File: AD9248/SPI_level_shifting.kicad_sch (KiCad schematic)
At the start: 9 parts, among them U10 TXB0101DBVR, U11 TXB0101DBVR, U12 TXB0101DBVR

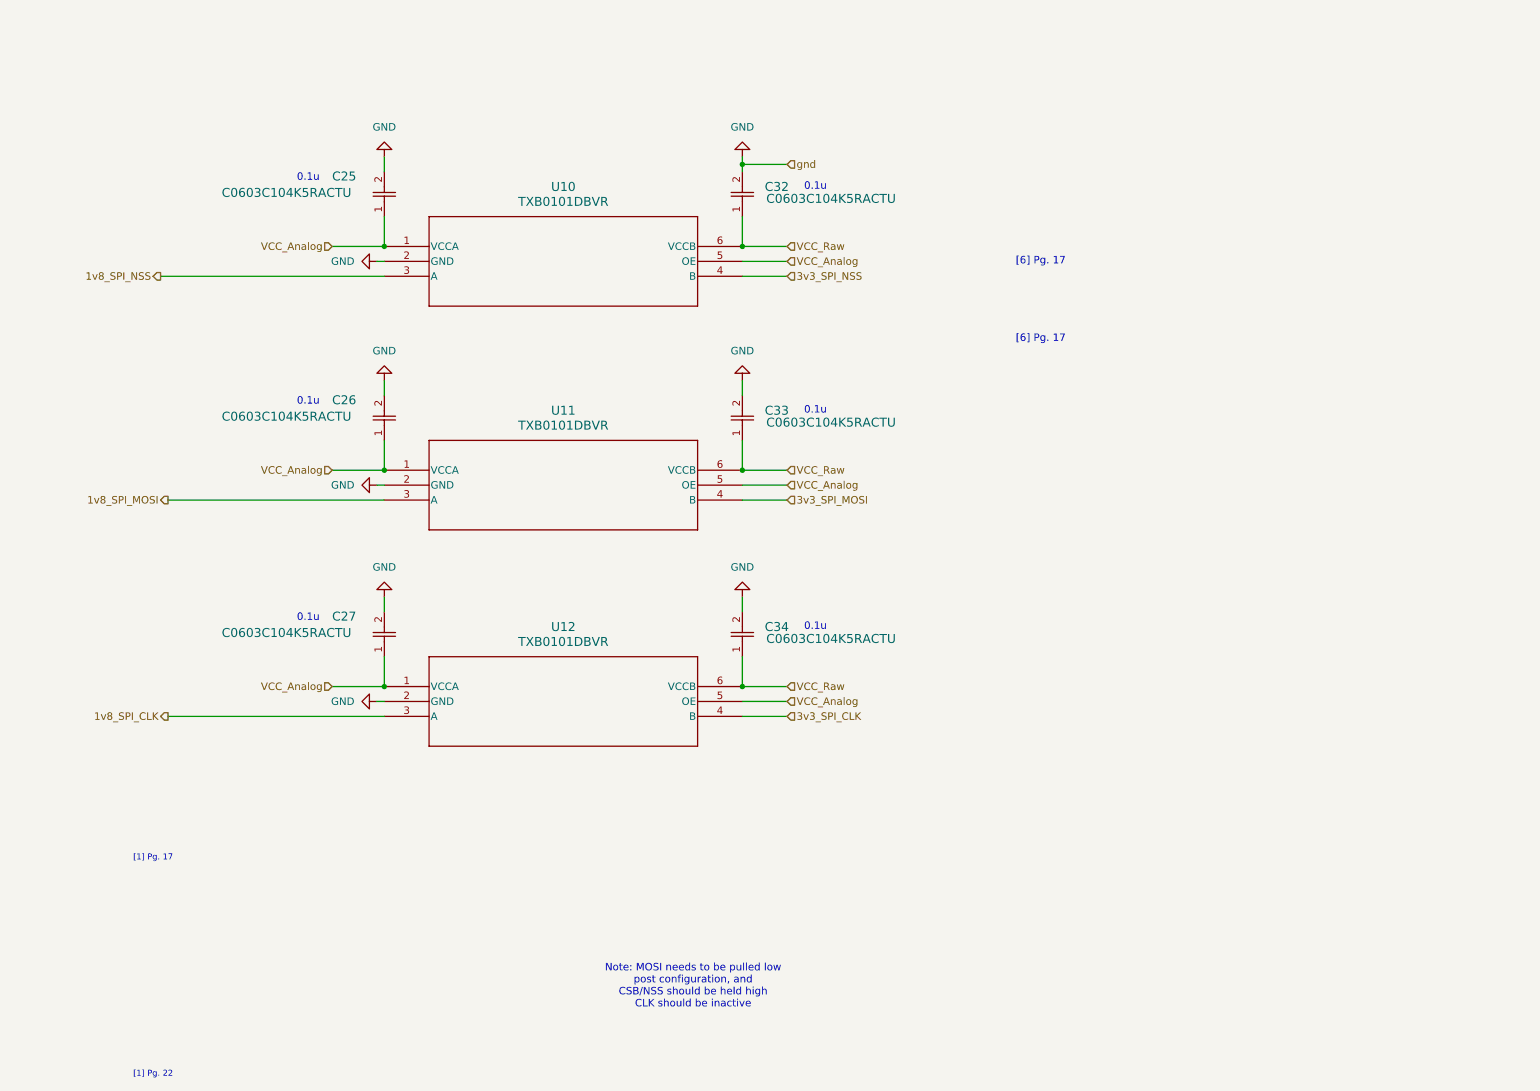
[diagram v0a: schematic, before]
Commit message: Finished and reviewed schematic, one change so far needs to be made: OE pin on level shifters must be externally toggled instead of tied to VCC. The IC requires VDDA/B to be fully ramped before pulling the OE high.
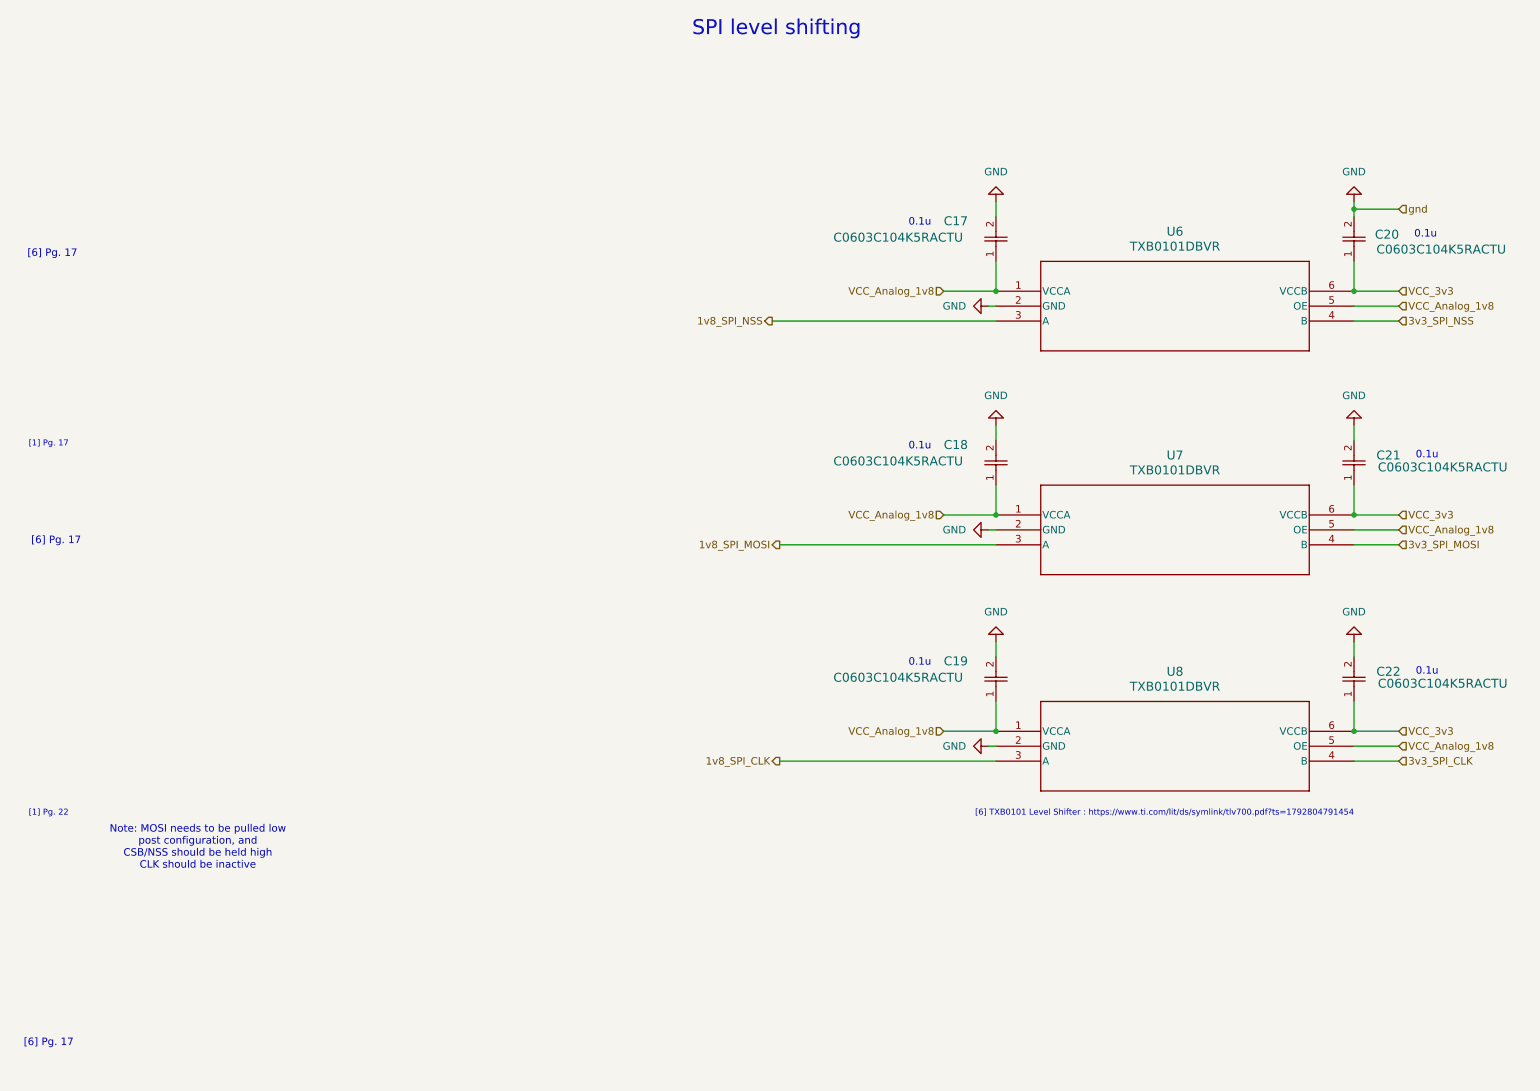
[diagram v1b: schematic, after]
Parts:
- renumbered C25 to C17, C26 to C18, C27 to C19, C32 to C20, C33 to C21, C34 to C22, U10 to U6, U11 to U7, U12 to U8
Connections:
- net VCC_Analog renamed VCC_Analog_1v8
- net VCC_Raw renamed VCC_3v3
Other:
- note added: "SPI level shifting"
- note added: "[6] TXB0101 Level Shifter : https://www.ti.com/lit/ds/symlink/tlv700.pdf?ts=1792804791454"
- moved on the sheet: C17, C18, C19, C20, C21, C22, U6, U7, U8
